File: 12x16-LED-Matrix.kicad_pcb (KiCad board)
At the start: 2 copper layers, 56 x 45 mm, 208 parts, among them J1 Conn_01x06, U1 IS31FL3733B

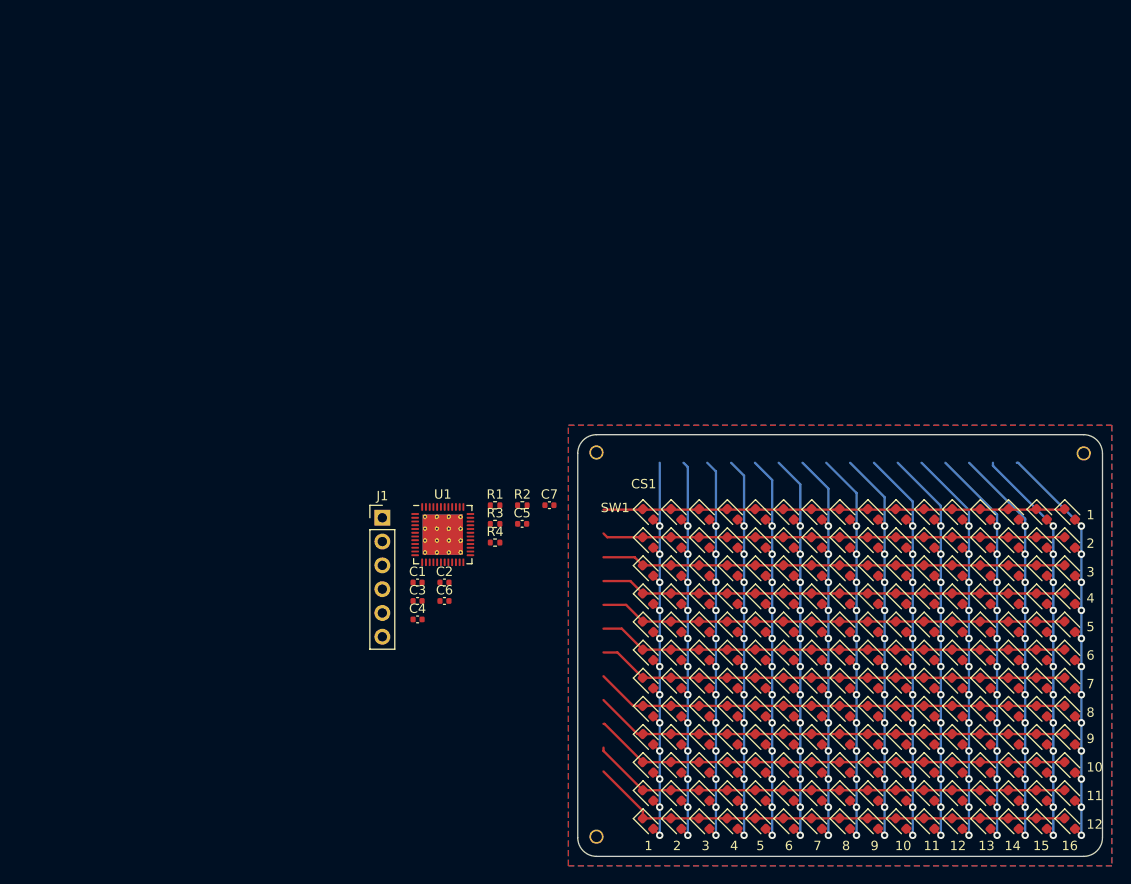
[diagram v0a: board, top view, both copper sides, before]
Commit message: Fully routed board
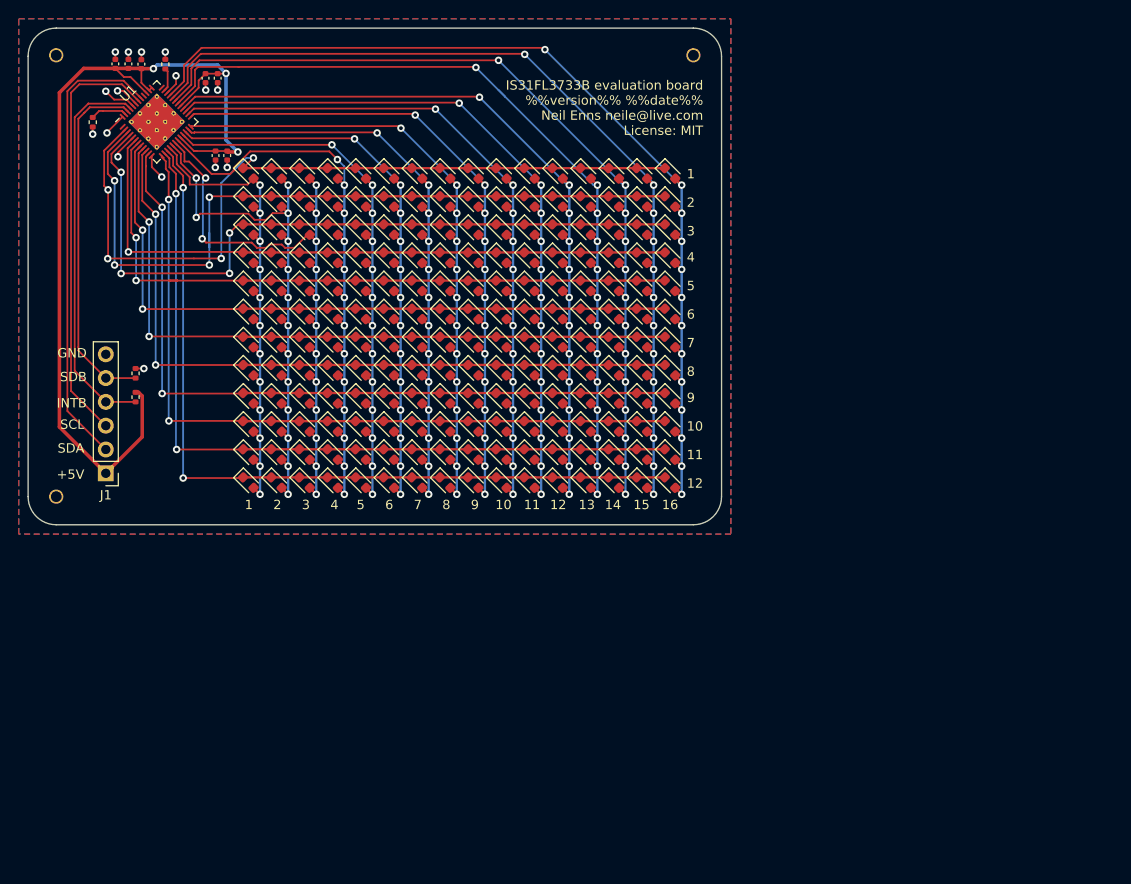
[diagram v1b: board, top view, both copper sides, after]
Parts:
- moved H1 71.6 mm to (19.3, 18.6)
- moved H3 68.1 mm to (19.3, 65.7)
- moved C6 66.5 mm to (27.1, 19.4), turned to 90 degrees
- moved C7 66.1 mm to (25.7, 19.4), turned to 90 degrees
- moved C3 64.4 mm to (28.4, 19.5), turned to 90 degrees
- moved R4 62.0 mm to (31.0, 19.5), turned to 90 degrees
- moved R3 60.7 mm to (23.2, 25.7), turned to 270 degrees
- moved C2 59.6 mm to (35.3, 21.0), turned to 270 degrees
- moved H2 59.5 mm to (87.3, 18.6)
- moved C5 57.6 mm to (36.6, 21.0), turned to 270 degrees
- moved D1 56.1 mm to (39.8, 31.1)
- moved D100 56.1 mm to (48.8, 49.1)
- moved D101 56.1 mm to (51.8, 49.1)
- moved D102 56.1 mm to (54.8, 49.1)
- moved D103 56.1 mm to (57.8, 49.1)
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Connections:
- net Net-(R3-Pad1) renamed /IICRST
- net Net-(R4-Pad1) renamed /ISET
- J1 pad 4: /SDB -> /INTB
- J1 pad 5: /INTB -> /SDB
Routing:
- net +5V: track 0.00 -> 102.9 mm, vias 0 -> 3
- net CS16: track 54.5 -> 108.6 mm, vias 12 -> 13
- net CS15: track 54.2 -> 105.1 mm, vias 12 -> 13
- net /SDA: track 0.00 -> 49.1 mm
- net CS14: track 54.0 -> 101.2 mm, vias 12 -> 13
- net /SCL: track 0.00 -> 45.4 mm
- net CS13: track 53.8 -> 98.4 mm, vias 12 -> 13
- net /INTB: track 0.00 -> 41.8 mm
- net /SDB: track 0.00 -> 38.3 mm
- net SW1: track 49.2 -> 86.6 mm, vias 0 -> 4
- net CS12: track 53.6 -> 90.4 mm, vias 12 -> 13
- net SW12: track 51.7 -> 87.2 mm, vias 0 -> 2
- net SW2: track 49.4 -> 82.9 mm, vias 0 -> 4
- net CS11: track 53.4 -> 86.7 mm, vias 12 -> 13
- net SW11: track 51.3 -> 84.3 mm, vias 0 -> 2
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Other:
- board size 56 x 45 mm -> 74 x 53 mm
- rule trace_min: 0.2 -> 0.127
- board text added: "+5V"
- board text added: "GND"
- board text added: "INTB"
- board text added: "IS31FL3733B evaluation board %%version%% %%date%% Neil Enns neile@live.com License: MIT"
- board text added: "SCL"
- board text added: "SDA"
- board text added: "SDB"
- board text removed: "%%version%% %%date%%"
- board text removed: "CS1"
- board text removed: "SW1"

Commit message: Switch to 47k ISET resistor
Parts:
- R4: value 20k -> 47k

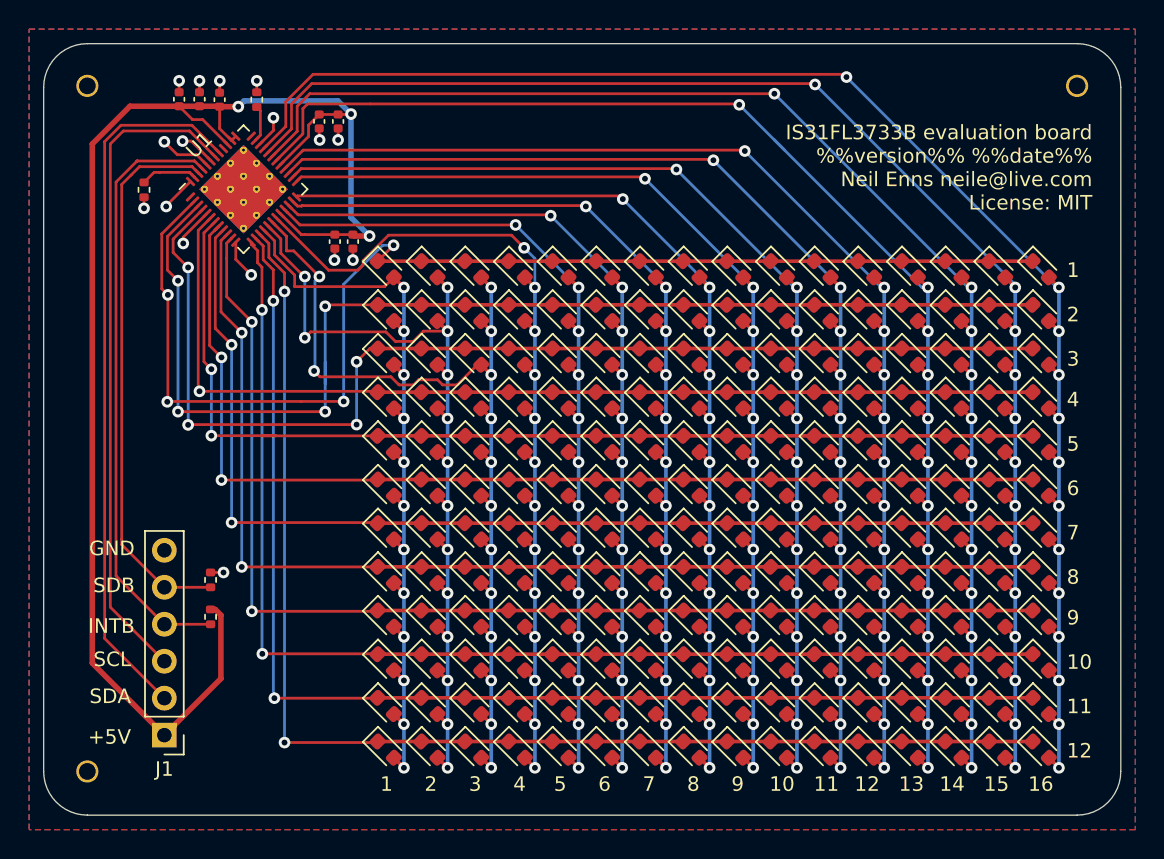
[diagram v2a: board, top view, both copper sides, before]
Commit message: Update components based on JLCPCB availability
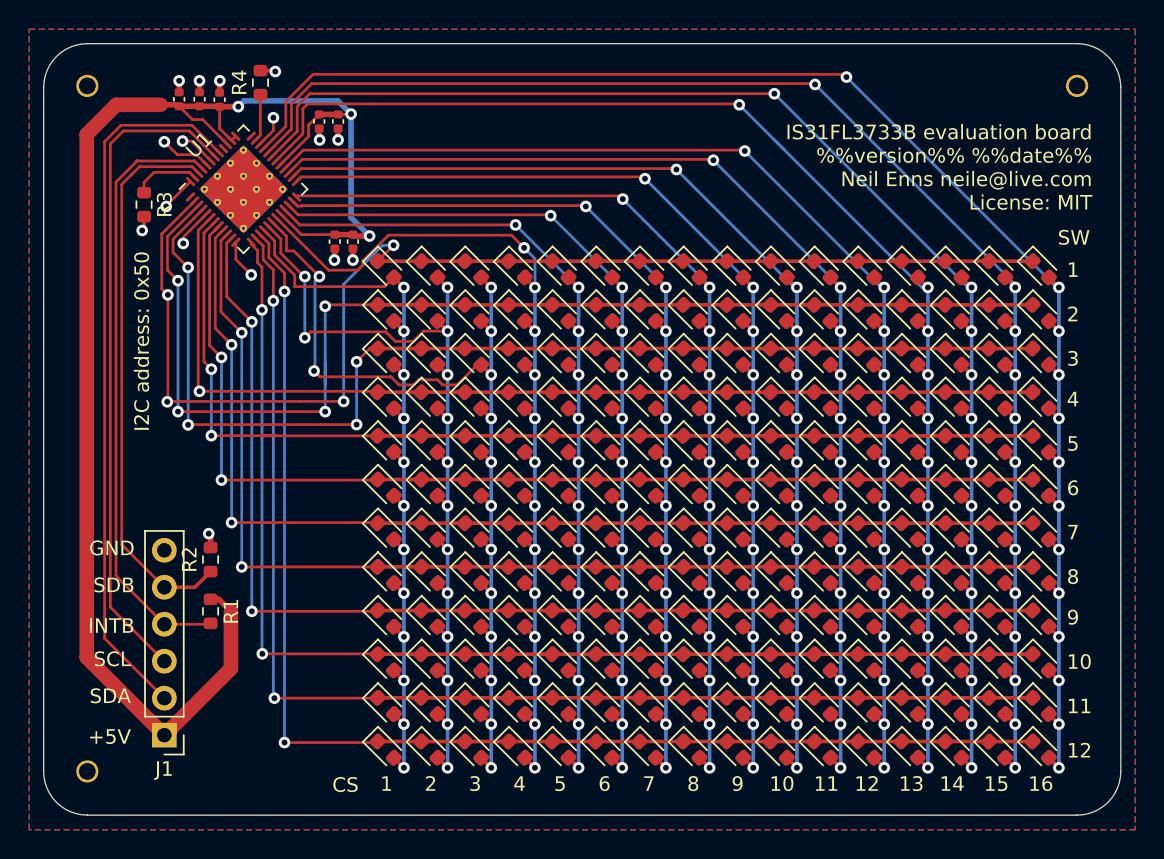
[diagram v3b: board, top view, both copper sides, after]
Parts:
- C4, C5, C6: value 0.1uF -> 100nf
- R1, R2, R3, R4: footprint Resistor_SMD:R_0402_1005Metric -> Resistor_SMD:R_0603_1608Metric
- moved R2 1.40 mm to (27.8, 51.1)
- moved R4 1.20 mm to (31.2, 18.3)
- moved R3 1.02 mm to (23.2, 26.7)
- moved R1 0.38 mm to (27.8, 54.6)
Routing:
- net +5V: track 102.9 -> 105.5 mm
- net /ISET: track 2.53 -> 3.29 mm
- net /IICRST: track 3.91 -> 4.61 mm
- net GND: track 24.2 -> 24.8 mm
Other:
- board text added: "CS"
- board text added: "I2C address: 0x50"
- board text added: "SW"

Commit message: Added some via stitching
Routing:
- net GND: vias 16 -> 28
